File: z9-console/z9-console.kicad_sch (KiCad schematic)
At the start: 4 parts

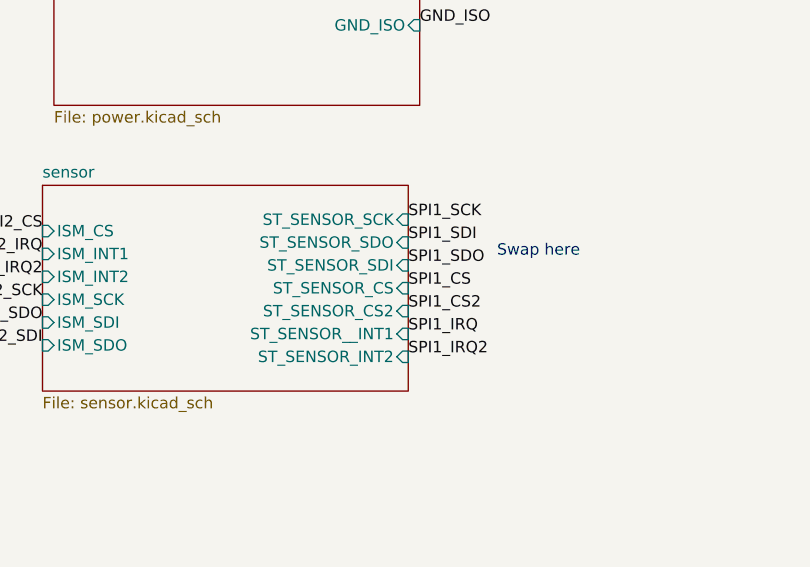
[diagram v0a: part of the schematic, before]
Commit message: Remove unused SPI labels and text from schematic for cleaner design
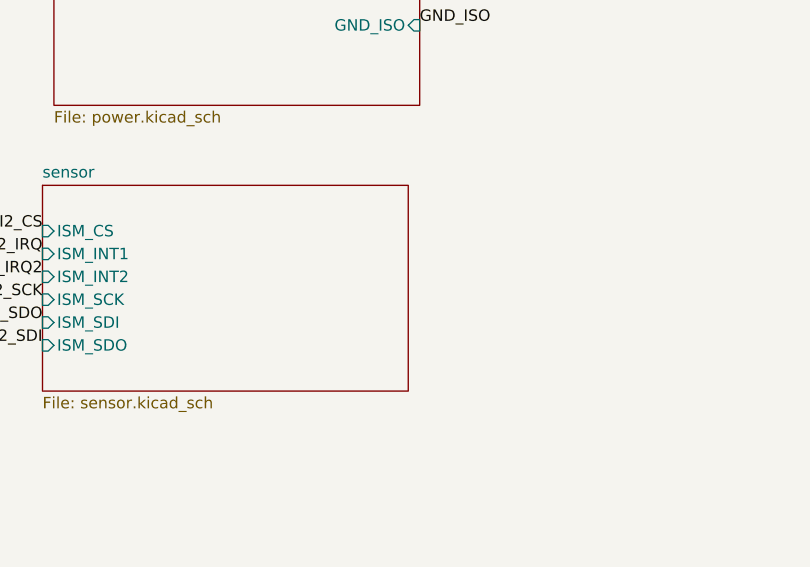
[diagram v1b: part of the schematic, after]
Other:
- sheet sensor ports: added none; removed ST_SENSOR_CS, ST_SENSOR_CS2, ST_SENSOR_INT2, ST_SENSOR_SCK, ST_SENSOR_SDI, ST_SENSOR_SDO, ST_SENSOR__INT1
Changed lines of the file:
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@@
-	(text "Swap here"
-		(exclude_from_sim no)
-		(at 107.188 180.086 0)
-		(effects
-			(font
-				(size 1.27 1.27)
-			)
-		)
-	)
 	(text "Swap here"
 		(exclude_from_sim no)
@@
 		)
 	)
-	(label "SPI1_IRQ"
-		(at 92.71 189.23 0)
-		(effects
-			(font
-				(size 1.27 1.27)
-			)
-			(justify left bottom)
-		)
-	)
 	(label "PE13"
 		(at 212.09 140.97 0)
@@
 		)
 	)
-	(label "SPI1_CS"
-		(at 92.71 184.15 0)
-		(effects
-			(font
-				(size 1.27 1.27)
-			)
-			(justify left bottom)
-		)
-	)
 	(label "LCD_RESET"
 		(at 222.25 232.41 0)
@@
 		)
 	)
-	(label "SPI1_IRQ2"
-		(at 92.71 191.77 0)
-		(effects
-			(font
-				(size 1.27 1.27)
-			)
-			(justify left bottom)
-		)
-	)
 	(label "GND_ISO"
 		(at 53.34 233.68 180)
@@
 		)
 	)
-	(label "SPI1_SDO"
-		(at 92.71 181.61 0)
-		(effects
-			(font
-				(size 1.27 1.27)
-			)
-			(justify left bottom)
-		)
-	)
 	(label "SPI4_SDO"
 		(at 95.25 71.12 0)
@@
 		)
 	)
-	(label "SPI1_SDI"
-		(at 92.71 179.07 0)
-		(effects
-			(font
-				(size 1.27 1.27)
-			)
-			(justify left bottom)
-		)
-	)
 	(label "SPI3_CS"
 		(at 222.25 184.15 0)
@@
 		)
 	)
-	(label "SPI1_SCK"
-		(at 92.71 176.53 0)
-		(effects
-			(font
-				(size 1.27 1.27)
-			)
-			(justify left bottom)
-		)
-	)
 	(label "SPI2_SDI"
 		(at 52.07 190.5 180)
@@
 	(label "SPI1_SDO"
 		(at 212.09 124.46 0)
-		(effects
-			(font
-				(size 1.27 1.27)
-			)
-			(justify left bottom)
-		)
-	)
-	(label "SPI1_CS2"
-		(at 92.71 186.69 0)
 		(effects
 			(font
@@
 			)
 		)
-		(pin "ST_SENSOR_SDO" input
-			(at 92.71 179.07 0)
-			(effects
-				(font
-					(size 1.27 1.27)
-				)
-				(justify right)
-			)
-		)
-		(pin "ST_SENSOR_SDI" input
-			(at 92.71 181.61 0)
-			(effects
-				(font
-					(size 1.27 1.27)
-				)
-				(justify right)
-			)
-		)
-		(pin "ST_SENSOR_CS" input
-			(at 92.71 184.15 0)
-			(effects
-				(font
-					(size 1.27 1.27)
-				)
-				(justify right)
-			)
-		)
-		(pin "ST_SENSOR_CS2" input
-			(at 92.71 186.69 0)
-			(effects
-				(font
-					(size 1.27 1.27)
-				)
-				(justify right)
-			)
-		)
-		(pin "ST_SENSOR__INT1" input
-			(at 92.71 189.23 0)
-			(effects
-				(font
-					(size 1.27 1.27)
-				)
-				(justify right)
-			)
-		)
-		(pin "ST_SENSOR_INT2" input
-			(at 92.71 191.77 0)
-			(effects
-				(font
-					(size 1.27 1.27)
-				)
-				(justify right)
-			)
-		)
-		(pin "ST_SENSOR_SCK" input
-			(at 92.71 176.53 0)
-			(effects
-				(font
-					(size 1.27 1.27)
-				)
-				(justify right)
-			)
-		)

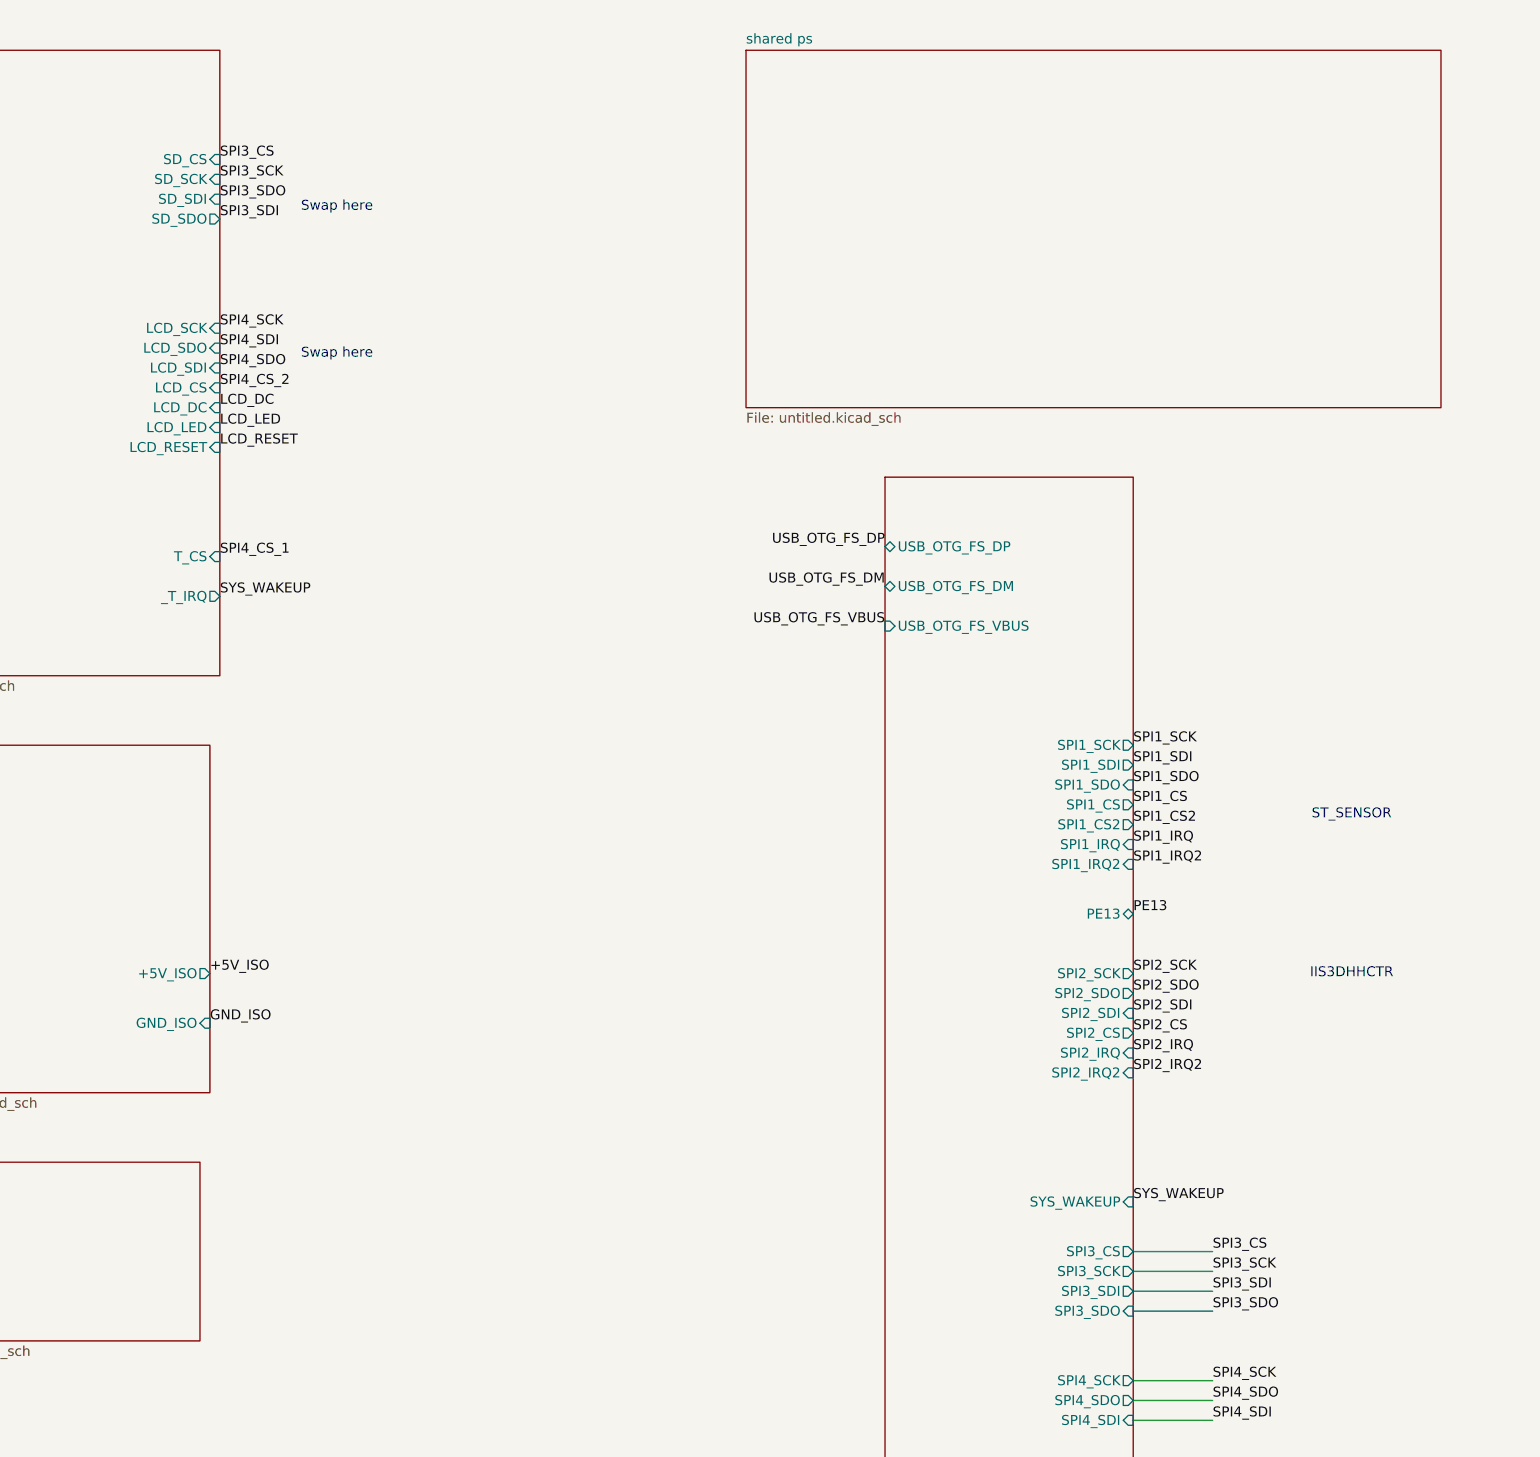
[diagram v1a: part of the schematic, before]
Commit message: Remove unused labels and wires from schematic SD Card junk
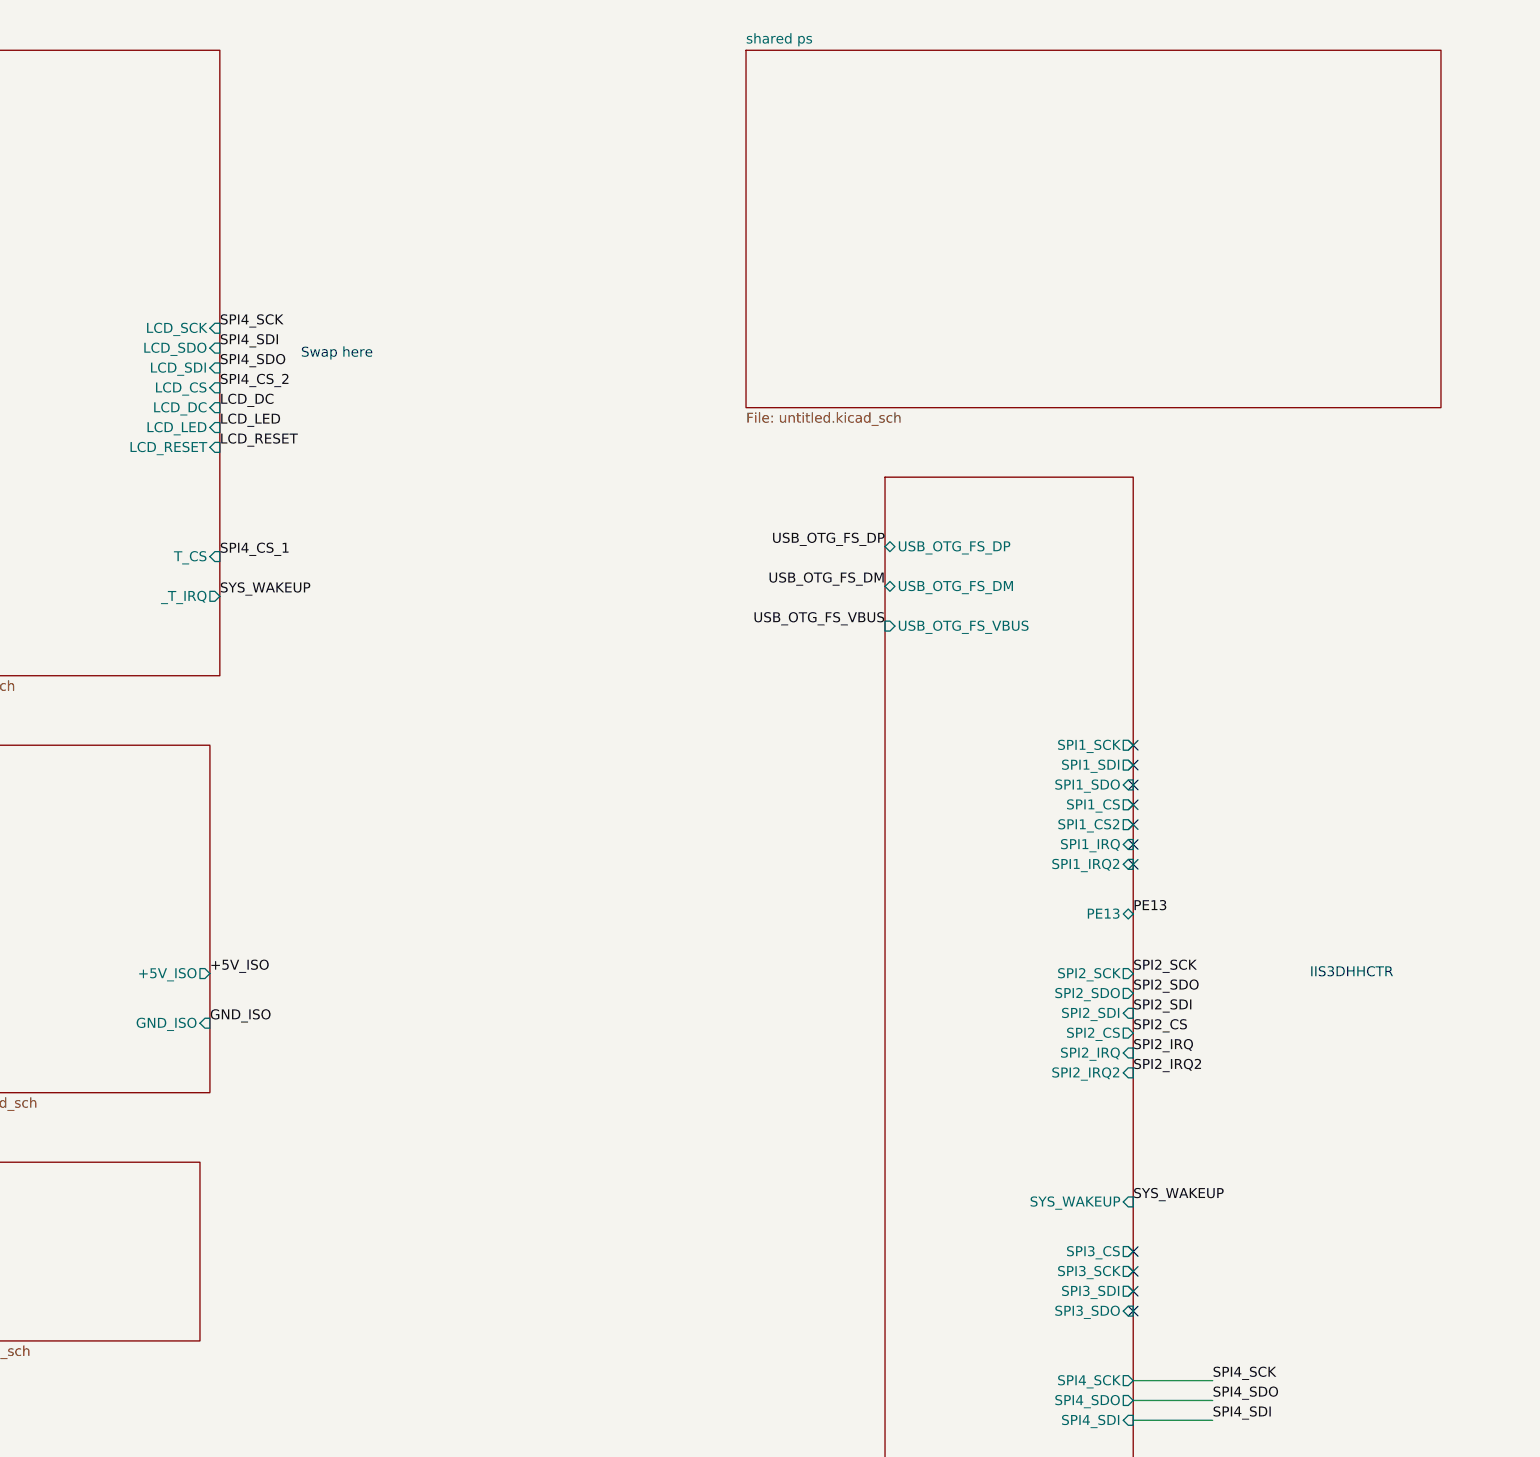
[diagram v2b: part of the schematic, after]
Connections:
- no-connect marks 1 -> 12
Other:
- sheet lcd ports: added none; removed SD_CS, SD_SCK, SD_SDI, SD_SDO
- note removed: "ST_SENSOR"
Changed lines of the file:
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@@
-		)
-	)
-	(text "ST_SENSOR"
-		(exclude_from_sim no)
-		(at 240.03 128.27 0)
-		(effects
-			(font
-				(size 1.27 1.27)
-			)
 		)
 	)
@@
 	(text "Swap here"
 		(exclude_from_sim no)
-		(at 110.236 50.546 0)
-		(effects
-			(font
-				(size 1.27 1.27)
-			)
-		)
-	)
-	(text "Swap here"
-		(exclude_from_sim no)
 		(at 38.1 188.468 0)
 		(effects
@@
 		(at 212.09 218.44)
 	)
+	(no_connect
+		(at 212.09 186.69)
+	)
+	(no_connect
+		(at 212.09 184.15)
+	)
+	(no_connect
+		(at 212.09 129.54)
+	)
+	(no_connect
+		(at 212.09 132.08)
+	)
+	(no_connect
+		(at 212.09 124.46)
+	)
+	(no_connect
+		(at 212.09 127)
+	)
+	(no_connect
+		(at 212.09 189.23)
+	)
+	(no_connect
+		(at 212.09 191.77)
+	)
+	(no_connect
+		(at 212.09 121.92)
+	)
+	(no_connect
+		(at 212.09 134.62)
+	)
+	(no_connect
+		(at 212.09 119.38)
+	)
 	(wire
 		(pts
@@
 	(wire
 		(pts
-			(xy 222.25 186.69) (xy 212.09 186.69)
+			(xy 212.09 224.79) (xy 222.25 224.79)
 		)
 		(stroke
@@
 	(wire
 		(pts
-			(xy 222.25 189.23) (xy 212.09 189.23)
+			(xy 212.09 227.33) (xy 222.25 227.33)
 		)
 		(stroke
@@
 	(wire
 		(pts
-			(xy 212.09 224.79) (xy 222.25 224.79)
+			(xy 212.09 200.66) (xy 222.25 200.66)
 		)
 		(stroke
@@
 	(wire
 		(pts
-			(xy 222.25 184.15) (xy 212.09 184.15)
+			(xy 212.09 215.9) (xy 222.25 215.9)
 		)
 		(stroke
@@
 	(wire
 		(pts
-			(xy 212.09 227.33) (xy 222.25 227.33)
+			(xy 212.09 229.87) (xy 222.25 229.87)
 		)
 		(stroke
@@
 	(wire
 		(pts
-			(xy 212.09 200.66) (xy 222.25 200.66)
+			(xy 222.25 213.36) (xy 212.09 213.36)
 		)
 		(stroke
@@
 		)
 	)
-	(wire
-		(pts
-			(xy 212.09 215.9) (xy 222.25 215.9)
-		)
-		(stroke
-			(width 0)
-			(type default)
-		)
-	)
-	(wire
-		(pts
-			(xy 222.25 191.77) (xy 212.09 191.77)
-		)
-		(stroke
-			(width 0)
-			(type default)
-		)
-	)
-	(wire
-		(pts
-			(xy 212.09 229.87) (xy 222.25 229.87)
-		)
-		(stroke
-			(width 0)
-			(type default)
-		)
-	)
-	(wire
-		(pts
-			(xy 222.25 213.36) (xy 212.09 213.36)
-		)
-		(stroke
-			(width 0)
-			(type default)
-		)
-	)
 	(label "SPI4_CS_1"
 		(at 222.25 213.36 0)
@@
 		)
 	)
-	(label "SPI3_SDI"
-		(at 95.25 52.07 0)
-		(effects
-			(font
-				(size 1.27 1.27)
-			)
-			(justify left bottom)
-		)
-	)
 	(label "USB_OTG_FS_DP"
 		(at 351.79 95.25 0)
@@
 		)
 	)
-	(label "SPI1_CS"
-		(at 212.09 127 0)
-		(effects
-			(font
-				(size 1.27 1.27)
-			)
-			(justify left bottom)
-		)
-	)
 	(label "SPI4_CS_2"
 		(at 95.25 73.66 0)
@@
 		)
 	)
-	(label "SPI3_CS"
-		(at 95.25 44.45 0)
-		(effects
-			(font
-				(size 1.27 1.27)
-			)
-			(justify left bottom)
-		)
-	)
 	(label "SPI2_IRQ"
 		(at 52.07 180.34 180)
@@
 		)
 	)
-	(label "SPI3_SDO"
-		(at 95.25 49.53 0)
-		(effects
-			(font
-				(size 1.27 1.27)
-			)
-			(justify left bottom)
-		)
-	)
 	(label "SPI4_SDO"
 		(at 95.25 71.12 0)
@@
 		)
 	)
-	(label "SPI3_SCK"
-		(at 95.25 46.99 0)
-		(effects
-			(font
-				(size 1.27 1.27)
-			)
-			(justify left bottom)
-		)
-	)
-	(label "SPI3_SDO"
-		(at 222.25 191.77 0)
-		(effects
-			(font
-				(size 1.27 1.27)
-			)
-			(justify left bottom)
-		)
-	)
 	(label "SPI4_SCK"
 		(at 222.25 200.66 0)
@@
 		)
 	)
-	(label "SPI3_SCK"
-		(at 222.25 186.69 0)
-		(effects
-			(font
-				(size 1.27 1.27)
-			)
-			(justify left bottom)
-		)
-	)
 	(label "LCD_RESET"
 		(at 95.25 81.28 0)
@@
 		)
 	)
-	(label "SPI3_CS"
-		(at 222.25 184.15 0)
-		(effects
-			(font
-				(size 1.27 1.27)
-			)
-			(justify left bottom)
-		)
-	)
 	(label "SYS_WAKEUP"
 		(at 212.09 177.8 0)
@@
 		)
 	)
-	(label "SPI1_SDI"
-		(at 212.09 121.92 0)
-		(effects
-			(font
-				(size 1.27 1.27)
-			)
-			(justify left bottom)
-		)
-	)
 	(label "CAN_H"
 		(at 53.34 229.87 180)
@@
 		)
 	)
-	(label "SPI1_IRQ2"
-		(at 212.09 134.62 0)
-		(effects
-			(font
-				(size 1.27 1.27)
-			)
-			(justify left bottom)
-		)
-	)
-	(label "SPI1_CS2"
-		(at 212.09 129.54 0)
-		(effects
-			(font
-				(size 1.27 1.27)
-			)
-			(justify left bottom)
-		)
-	)
 	(label "CAN1_RX"
 		(at 180.34 224.79 180)
@@
 		)
 	)
-	(label "SPI1_SDO"
-		(at 212.09 124.46 0)
-		(effects
-			(font
-				(size 1.27 1.27)
-			)
-			(justify left bottom)
-		)
-	)
 	(label "CAN1_RX"
 		(at 299.72 30.48 180)
@@
 		)
 	)
-	(label "SPI3_SDI"
-		(at 222.25 189.23 0)
-		(effects
-			(font
-				(size 1.27 1.27)
-			)
-			(justify left bottom)
-		)
-	)
-	(label "SPI1_IRQ"
-		(at 212.09 132.08 0)
-		(effects
-			(font
-				(size 1.27 1.27)
-			)
-			(justify left bottom)
-		)
-	)
 	(label "SPI2_IRQ2"
 		(at 212.09 161.29 0)
@@
 	(label "USB_OTG_FS_DM"
 		(at 351.79 91.44 0)
-		(effects
-			(font
-				(size 1.27 1.27)
-			)
-			(justify left bottom)
-		)
-	)
-	(label "SPI1_SCK"
-		(at 212.09 119.38 0)
 		(effects
 			(font
@@
 			(effects
 				(font
-					(size 1.27 1.27)
-				)
-				(justify right)
-			)
-		)
-		(pin "SD_CS" input
-			(at 95.25 44.45 0)
-			(effects
-				(font
-					(size 1.27 1.27)
-				)
-				(justify right)
-			)
-		)
-		(pin "SD_SCK" input
-			(at 95.25 46.99 0)
-			(effects
-				(font
-					(size 1.27 1.27)
-				)
-				(justify right)
-			)
-		)
-		(pin "SD_SDI" input
-			(at 95.25 49.53 0)
-			(effects
-				(font
-					(size 1.27 1.27)
-				)
-				(justify right)
-			)
-		)
-		(pin "SD_SDO" output
-			(at 95.25 52.07 0)
-			(effects
-				(font
